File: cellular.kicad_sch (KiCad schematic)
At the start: 0 parts

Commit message: schem: add sim7080G lte module
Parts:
- added U13: SIM7080G, RF_GSM:SIMCom_SIM800C, symbol GLCS:SIM7080G
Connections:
- new net: U13.28 (NC), U13.29 (NC), U13.46 (NC), U13.47 (NC), U13.52 (NC), U13.53 (NC), U13.54 (NC), U13.55 (NC), U13.56 (NC)
- new net GND: U13.13 (GND), U13.19 (GND), U13.21 (GND), U13.27 (GND), U13.30 (GND), U13.31 (GND), U13.33 (GND), U13.36 (GND), U13.37 (GND), U13.45 (GND), U13.63 (GND), U13.66 (GND), U13.67 (GND), U13.69 (GND), U13.70 (GND), U13.71 (GND), U13.72 (GND), U13.73 (GND), U13.74 (GND), U13.75 (GND), U13.76 (GND), U13.77 (GND), U13.8 (GND)
- new net VBAT: U13.34 (VBAT), U13.35 (VBAT)

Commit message: schem: add lte decoupling caps
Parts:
- added C40, C41: 1u, Capacitor_SMD:C_0402_1005Metric, symbol Device:C
- added C42, C43, C44, C45, C46: 10u, Capacitor_SMD:C_0402_1005Metric, symbol Device:C
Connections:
- net GND: now also C40.1, C41.1, C42.2, C43.2, C44.2, C45.2, C46.2
- net +1V8: now reaches U13.40 (VDD_EXT)
- net +1V8: now also C40.2
- net VBAT renamed +3V8
- net +3V8: now also C41.2, C42.1, C43.1, C44.1, C45.1, C46.1

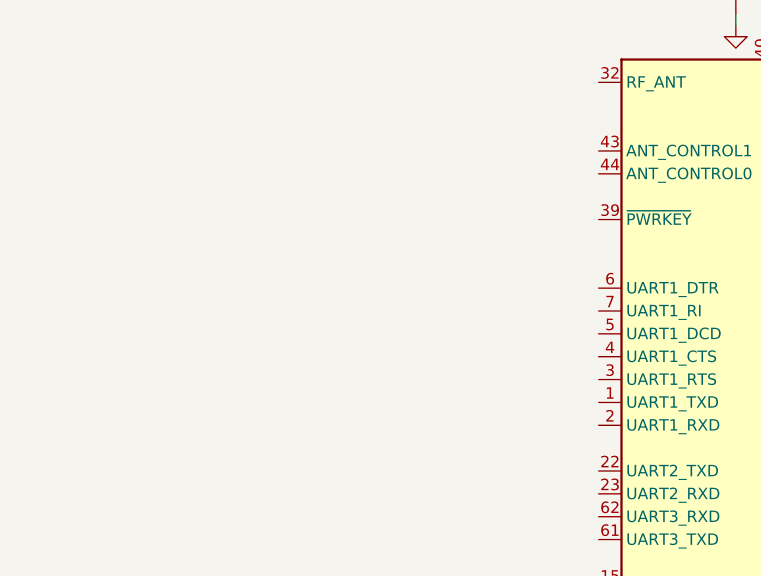
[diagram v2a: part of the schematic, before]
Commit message: schem: add lte pwr control
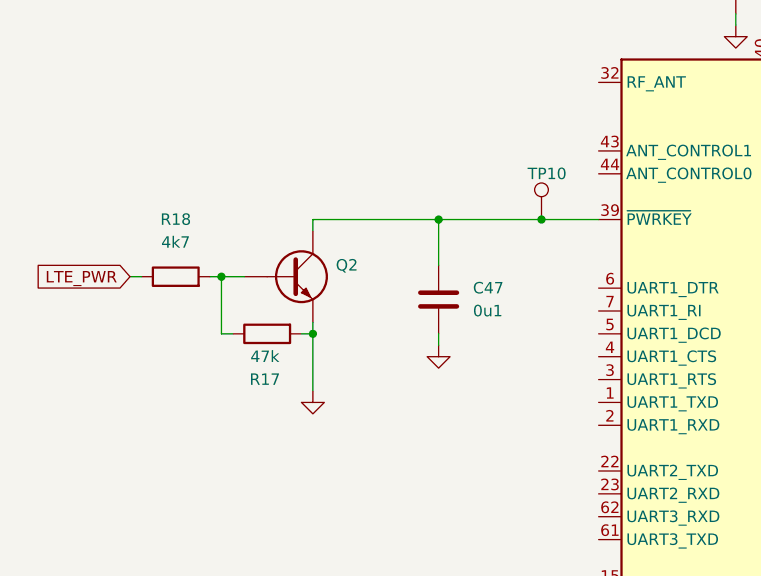
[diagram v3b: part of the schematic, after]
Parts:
- added C47: 0u1, Capacitor_SMD:C_0402_1005Metric, symbol Device:C
- added Q2: MMBT3904, Package_QFP:TQFP-44_10x10mm_P0.8mm, symbol Device:Q_NPN
- added R17: 47k, symbol Device:R
- added R18: 4k7, symbol Device:R
- added TP10: TestPoint, TestPoint:TestPoint_Pad_D2.0mm, symbol Connector:TestPoint
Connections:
- net GND: now also C47.1, Q2.E, R17.2
- net at U13.39 (~{PWRKEY}): now also C47.2, Q2.C, TP10.1
- new net: Q2.B, R17.1, R18.2
- new net LTE_PWR: R18.1

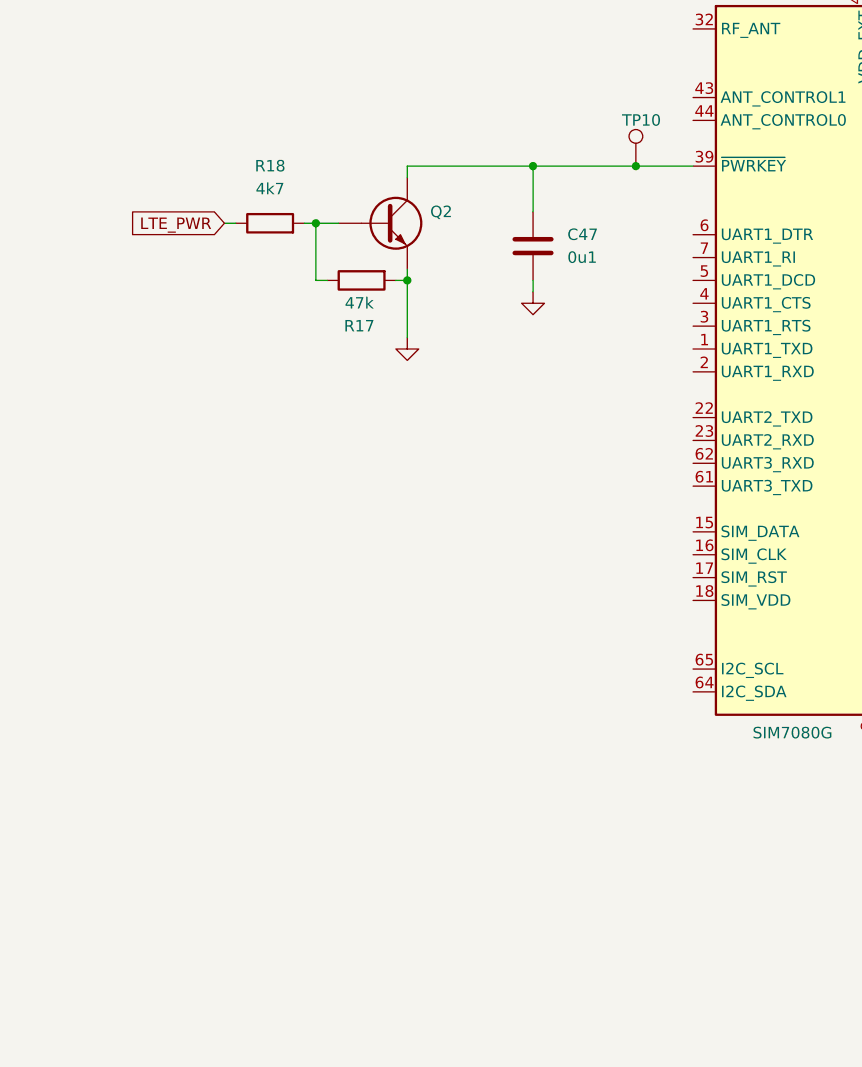
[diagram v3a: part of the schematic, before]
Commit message: schem: add level shifter
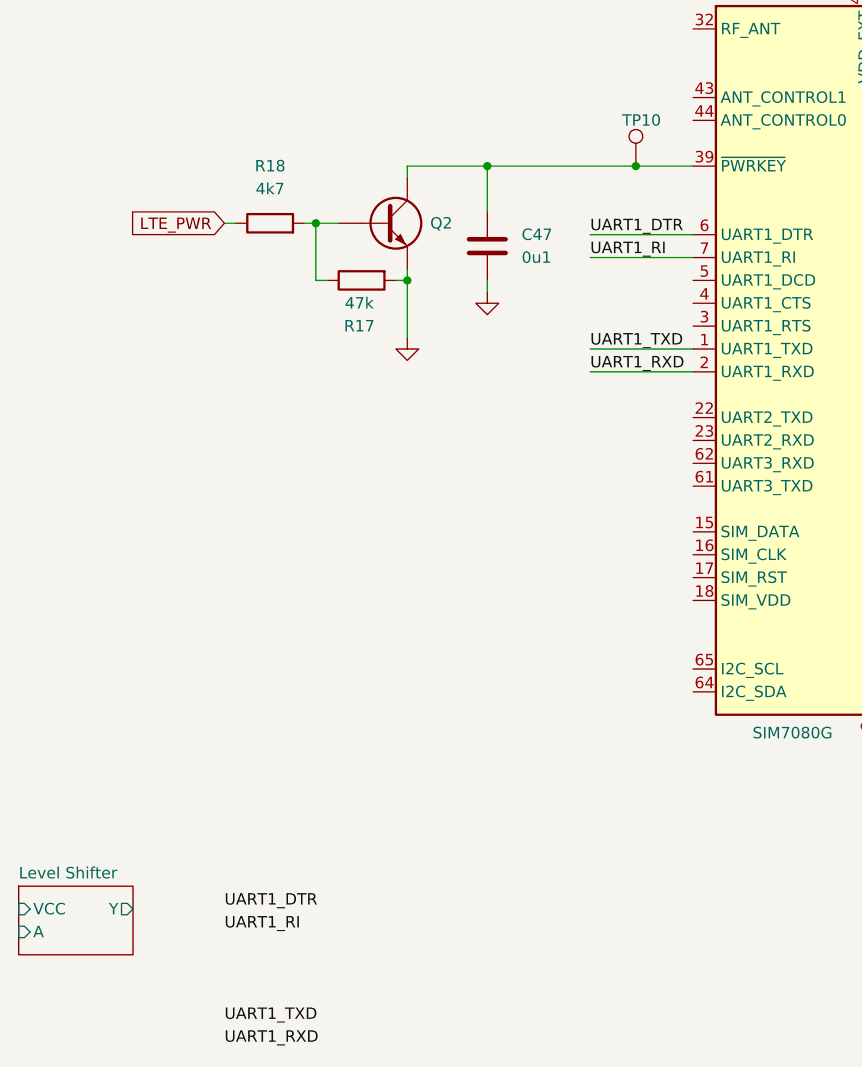
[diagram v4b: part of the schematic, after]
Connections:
- net UART1_TXD: now reaches U13.1 (UART1_TXD)
- net UART1_RXD: now reaches U13.2 (UART1_RXD)
- net UART1_DTR: now reaches U13.6 (UART1_DTR)
- net UART1_RI: now reaches U13.7 (UART1_RI)
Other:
- added sheet Level Shifter (level-shifter.kicad_sch)
- moved on the sheet: C47
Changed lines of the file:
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@@
 	)
 	(junction
-		(at 114.3 66.04)
+		(at 109.22 66.04)
 		(diameter 0)
 		(color 0 0 0 0)
@@
 	(wire
 		(pts
-			(xy 100.33 66.04) (xy 114.3 66.04)
+			(xy 100.33 66.04) (xy 125.73 66.04)
+		)
+		(stroke
+			(width 0)
+			(type default)
+		)
+	)
+	(wire
+		(pts
+			(xy 120.65 76.2) (xy 132.08 76.2)
 		)
 		(stroke
@@
 	(wire
 		(pts
+			(xy 120.65 88.9) (xy 132.08 88.9)
+		)
+		(stroke
+			(width 0)
+			(type default)
+		)
+	)
+	(wire
+		(pts
 			(xy 176.53 34.29) (xy 181.61 34.29)
 		)
@@
 	(wire
 		(pts
+			(xy 120.65 73.66) (xy 132.08 73.66)
+		)
+		(stroke
+			(width 0)
+			(type default)
+		)
+	)
+	(wire
+		(pts
 			(xy 100.33 67.31) (xy 100.33 66.04)
 		)
@@
 	(wire
 		(pts
-			(xy 114.3 66.04) (xy 114.3 71.12)
+			(xy 109.22 66.04) (xy 109.22 71.12)
 		)
 		(stroke
@@
 	(wire
 		(pts
+			(xy 120.65 86.36) (xy 132.08 86.36)
+		)
+		(stroke
+			(width 0)
+			(type default)
+		)
+	)
+	(wire
+		(pts
 			(xy 91.44 78.74) (xy 90.17 78.74)
 		)
@@
 	(wire
 		(pts
-			(xy 114.3 66.04) (xy 125.73 66.04)
-		)
-		(stroke
-			(width 0)
-			(type default)
-		)
-	)
-	(wire
-		(pts
 			(xy 171.45 44.45) (xy 171.45 43.18)
 		)
@@
 	(wire
 		(pts
-			(xy 114.3 78.74) (xy 114.3 80.01)
+			(xy 109.22 78.74) (xy 109.22 80.01)
 		)
 		(stroke
@@
 			(width 0)
 			(type default)
+		)
+	)
+	(label "UART1_DTR"
+		(at 120.65 73.66 0)
+		(effects
+			(font
+				(size 1.27 1.27)
+			)
+			(justify left bottom)
+		)
+	)
+	(label "UART1_DTR"
+		(at 80.01 148.59 0)
+		(effects
+			(font
+				(size 1.27 1.27)
+			)
+			(justify left bottom)
+		)
+	)
+	(label "UART1_RXD"
+		(at 80.01 163.83 0)
+		(effects
+			(font
+				(size 1.27 1.27)
+			)
+			(justify left bottom)
+		)
+	)
+	(label "UART1_TXD"
+		(at 80.01 161.29 0)
+		(effects
+			(font
+				(size 1.27 1.27)
+			)
+			(justify left bottom)
+		)
+	)
+	(label "UART1_RXD"
+		(at 120.65 88.9 0)
+		(effects
+			(font
+				(size 1.27 1.27)
+			)
+			(justify left bottom)
+		)
+	)
+	(label "UART1_TXD"
+		(at 120.65 86.36 0)
+		(effects
+			(font
+				(size 1.27 1.27)
+			)
+			(justify left bottom)
+		)
+	)
+	(label "UART1_RI"
+		(at 120.65 76.2 0)
+		(effects
+			(font
+				(size 1.27 1.27)
+			)
+			(justify left bottom)
+		)
+	)
+	(label "UART1_RI"
+		(at 80.01 151.13 0)
+		(effects
+			(font
+				(size 1.27 1.27)
+			)
+			(justify left bottom)
 		)
 	)
@@
 		(fields_autoplaced yes)
 		(property "Reference" "Q2"
-			(at 102.87 71.1199 0)
+			(at 102.87 72.3899 0)
 			(show_name no)
 			(do_not_autoplace no)
@@
 	(symbol
 		(lib_id "Device:C")
-		(at 114.3 74.93 180)
+		(at 109.22 74.93 180)
 		(unit 1)
 		(body_style 1)
@@
 		(fields_autoplaced yes)
 		(property "Reference" "C47"
-			(at 118.11 73.6599 0)
+			(at 113.03 73.6599 0)
 			(show_name no)
 			(do_not_autoplace no)
@@
 		)
 		(property "Value" "0u1"
-			(at 118.11 76.1999 0)
+			(at 113.03 76.1999 0)
 			(show_name no)
 			(do_not_autoplace no)
@@
 		)
 		(property "Footprint" "Capacitor_SMD:C_0402_1005Metric"
-			(at 113.3348 71.12 0)
+			(at 108.2548 71.12 0)
 			(hide yes)
 			(show_name no)
@@
 		)
 		(property "Datasheet" ""
-			(at 114.3 74.93 0)
+			(at 109.22 74.93 0)
 			(hide yes)
 			(show_name no)
@@
 		)
 		(property "Description" "Unpolarized capacitor"
-			(at 114.3 74.93 0)
+			(at 109.22 74.93 0)
 			(hide yes)
 			(show_name no)
@@
 		)
 		(property "Manufacturer" "Samsung Electro-Mechanics "
-			(at 114.3 74.93 90)
+			(at 109.22 74.93 90)
 			(hide yes)
 			(show_name no)
@@
 		)
 		(property "Manufacturer Part Number" "CL05B104KB54PNC"
-			(at 114.3 74.93 90)
+			(at 109.22 74.93 90)
 			(hide yes)
 			(show_name no)
@@
 		)
 		(property "Basic" "Y"
-			(at 114.3 74.93 90)
+			(at 109.22 74.93 90)
 			(hide yes)
 			(show_name no)
@@
 		)
 		(property "JLCPCB Part #" "C307331"
-			(at 114.3 74.93 90)
+			(at 109.22 74.93 90)
 			(hide yes)
 			(show_name no)
@@
 		)
 		(property "KLC_S3.3" ""
-			(at 114.3 74.93 90)
+			(at 109.22 74.93 90)
 			(hide yes)
 			(show_name no)
@@
 		)
 		(property "KLC_S4.1" ""
-			(at 114.3 74.93 90)
+			(at 109.22 74.93 90)
 			(hide yes)
 			(show_name no)
@@
 	(symbol
 		(lib_id "power:GND")
-		(at 114.3 80.01 0)
+		(at 109.22 80.01 0)
 		(unit 1)
 		(body_style 1)
@@
 		(fields_autoplaced yes)
 		(property "Reference" "#PWR099"
-			(at 114.3 86.36 0)
+			(at 109.22 86.36 0)
 			(hide yes)
 			(show_name no)
@@
 		)
 		(property "Value" "GND"
-			(at 114.3 85.09 0)
+			(at 109.22 85.09 0)
 			(hide yes)
 			(show_name no)
@@
 		)
 		(property "Footprint" "RF_GSM:SIMCom_SIM800C"
-			(at 114.3 80.01 0)
+			(at 109.22 80.01 0)
 			(hide yes)
 			(show_name no)
@@
 		)
 		(property "Datasheet" ""
-			(at 114.3 80.01 0)
+			(at 109.22 80.01 0)
 			(hide yes)
 			(show_name no)
@@
 		)
 		(property "Description" "Power symbol creates a global label with name \"GND\" , ground"
-			(at 114.3 80.01 0)
+			(at 109.22 80.01 0)
 			(hide yes)
 			(show_name no)
@@
 				)
 			)
+		)
+	)
+	(sheet
+		(at 57.15 146.05)
+		(size 12.7 7.62)
+		(exclude_from_sim no)
+		(in_bom yes)
+		(on_board yes)
+		(dnp no)
+		(fields_autoplaced yes)
+		(stroke
+			(width 0.1524)
+			(type solid)
+		)
+		(fill
+			(color 0 0 0 0)
+		)
+		(property "Sheetname" "Level Shifter"
+			(at 57.15 145.3384 0)
+			(show_name no)
+			(do_not_autoplace no)
+			(effects
+				(font
+					(size 1.27 1.27)
+				)
+				(justify left bottom)
+			)
+		)
+		(property "Sheetfile" "level-shifter.kicad_sch"
+			(at 57.15 154.2546 0)
+			(hide yes)
+			(show_name no)
+			(do_not_autoplace no)
+			(effects
+				(font
+					(size 1.27 1.27)
+				)
+				(justify left top)
+			)
+		)
+		(pin "A" input
+			(at 57.15 151.13 180)
+			(effects
+				(font
+					(size 1.27 1.27)
+				)
+				(justify left)
+			)
+		)
+		(pin "VCC" input
+			(at 57.15 148.59 180)
+			(effects
+				(font
+					(size 1.27 1.27)
+				)
+				(justify left)
+			)
+		)
+		(pin "Y" output
+			(at 69.85 148.59 0)
+			(effects
+				(font
+					(size 1.27 1.27)
+				)
+				(justify right)
+			)
+		)
+		(instances
+			(project "s6tm-detect-cb-2"
+				(path "/f4a18219-a653-4da9-9eb6-662d05c28432/2e4c8b7c-4e07-4d89-a615-6ea5caa4da61"
+					(page "5")
+				)
+			)

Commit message: schem: add sim uart level shifters
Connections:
- net UART1_RTS: now reaches U13.3 (UART1_RTS)
- net UART1_CTS: now reaches U13.4 (UART1_CTS)
- net UART1_RI: no longer names the net of U13.7 (UART1_RI)
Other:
- added sheet Level Shifter1 (level-shifter.kicad_sch)
- added sheet Level Shifter2 (level-shifter.kicad_sch)
- added sheet Level Shifter3 (level-shifter.kicad_sch)
- added sheet Level Shifter4 (level-shifter.kicad_sch)

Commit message: schem: add status and netlight
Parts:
- added D11: GREEN, LED_SMD:LED_0805_2012Metric, symbol Device:LED
- added D12: WHITE, LED_SMD:LED_0603_1608Metric, symbol Device:LED
- added Q3, Q4: MMBT3904, Package_QFP:TQFP-44_10x10mm_P0.8mm, symbol Device:Q_NPN
- added R19, R34: 4k7, symbol Device:R
- added R31, R35: 47k, symbol Device:R
- added R32, R36: 5k1, Resistor_SMD:R_0402_1005Metric, symbol Device:R
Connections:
- net +3V3: now also R32.1, R36.1
- net GND: now also Q3.E, Q4.E, R31.2, R35.2
- net NETLIGHT: now reaches U13.41 (NETLIGHT)
- net NETLIGHT: now also R34.1
- net STATUS: now reaches U13.42 (STATUS)
- net STATUS: now also R19.1
- new net: Q3.B, R19.2, R31.1
- new net: Q4.B, R34.2, R35.1
- new net: D12.1 (K), Q4.C
- new net: D12.2 (A), R36.2
- new net: D11.1 (K), Q3.C
- new net: D11.2 (A), R32.2

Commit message: schem: add modem usb connector
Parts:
- added D13, D14, D15: H5VU10U, GLCS:Diode_DFN1006, symbol GLCS:H5VU10U
- added J2: USB_C_Receptacle_USB2.0_14P, Connector_USB:USB_C_Receptacle_HRO_TYPE-C-31-M-12, symbol Connector:USB_C_Receptacle_USB2.0_14P
- added R33, R37: 5k1, Resistor_SMD:R_0402_1005Metric, symbol Device:R
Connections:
- net GND: now also D13.2 (A), D14.2 (A), D15.2 (A), J2.A1 (GND), J2.A12 (GND), J2.B1 (GND), J2.B12 (GND), J2.SH (SHIELD), R33.1, R37.1
- net VBUS: now reaches U13.24 (USB_VBUS)
- net VBUS: now also D14.1 (K), J2.A4 (VBUS), J2.A9 (VBUS), J2.B4 (VBUS), J2.B9 (VBUS)
- net D+: now reaches U13.25 (USB_DP)
- net D+: now also D15.1 (K), J2.A6 (D+), J2.B6 (D+)
- net D-: now reaches U13.26 (USB_DM)
- net D-: now also D13.1 (K), J2.A7 (D-), J2.B7 (D-)
- new net: J2.B5 (CC2), R37.2
- new net: J2.A5 (CC1), R33.2
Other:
- note added: "USB/MODEM"

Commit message: schem: add modem no connects
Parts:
- added SW4: SW_Push, Button_Switch_SMD:SW_SPST_TS-1088-xR020, symbol Switch:SW_Push
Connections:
- net +1V8: now also SW4.2
- net at U13.20 (USB_BOOT): now also SW4.1
- no-connect marks 0 -> 16
